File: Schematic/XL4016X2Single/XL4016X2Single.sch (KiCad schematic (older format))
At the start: 68 parts, among them J1 Solar panel, J10 SD_Micro_5V, J2 Buck1_IN, J3 LOAD, J4 Buck1_OUT, J5 Buck2_IN, J6 Buck2_OUT, J7 Battery, J8 Temperature, J9 Jack-DC, Q1 IRF4905, Q10 IRF4905, Q11 2N3906, Q12 2N3906, Q13 2N3904, Q2 IRF4905, Q3 2N3906, Q4 2N3906, Q5 2N3904, Q6 IRF4905, Q7 2N3906, Q8 2N3906, Q9 IRF4905, SW1 Backlight control, U1 XL4016_DC-DC_module, U11 DS18B20, U12 DS1307_RTC, U2 ACS712module, U3 XL4016_DC-DC_module, U4 ACS712module, U5 MP2307_DC-DC_module, U6 LCDSerial2004, U7 DS18B20, U8 ArduinoNano

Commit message: added RTC and SD to Fritzing. Minor updates to KiCad schematic.
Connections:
- net GNDPWR: no longer C1.1.2, C1.2.2, C1.3.2, C1.4.2, D3.2 (A2), J1.2 (Pin_2), J2.2 (Pin_2), J5.2 (Pin_2)
- new net SOLARGND: C1.1.2, C1.2.2, C1.3.2, C1.4.2, D3.2 (A2), J1.2 (Pin_2), J2.2 (Pin_2), J5.2 (Pin_2)
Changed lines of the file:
@@
 Sheet 1 1
 Title "XL4016X2Single"
-Date "2018-04-11"
-Rev "Initial issue"
+Date "2018-04-12"
+Rev "V2"
 Comp "farmerkeith"
 Comment1 ""
@@
 $EndComp
 $Comp
-L GNDPWR #PWR3
-U 1 1 5ACD67FC
-P 900 1250
-F 0 "#PWR3" H 900 1050 50  0001 C CNN
-F 1 "GNDPWR" H 900 1120 50  0000 C CNN
-F 2 "" H 900 1200 50  0001 C CNN
-F 3 "" H 900 1200 50  0001 C CNN
-	1    900  1250
-	1    0    0    -1
-$EndComp
-$Comp
 L GNDPWR #PWR13
 U 1 1 5ACD67FD
@@
 $EndComp
 Wire Wire Line
-	1350 1050 1850 1050
-Wire Wire Line
-	900  750  2100 750
+	1350 1050 1550 1050
+Wire Wire Line
+	1550 1050 1850 1050
+Wire Wire Line
+	900  750  1100 750
+Wire Wire Line
+	1100 750  1350 750
+Wire Wire Line
+	1350 750  2100 750
 $Comp
 L GND #PWR4
@@
 $EndComp
 $Comp
-L GNDPWR #PWR8
-U 1 1 5ACD6807
-P 3200 1950
-F 0 "#PWR8" H 3200 1750 50  0001 C CNN
-F 1 "GNDPWR" H 3200 1820 50  0000 C CNN
-F 2 "" H 3200 1900 50  0001 C CNN
-F 3 "" H 3200 1900 50  0001 C CNN
-	1    3200 1950
-	1    0    0    -1
-$EndComp
-$Comp
 L ACS712module U2
 U 1 1 5ACD6808
@@
 Connection ~ 9800 3650
 Wire Wire Line
-	2550 750  4500 750
+	2550 750  2900 750
+Wire Wire Line
+	2900 750  3400 750
+Wire Wire Line
+	3400 750  4500 750
 $Comp
 L XL4016_DC-DC_module U3
@@
 L GNDPWR #PWR1
 U 1 1 5ACD6813
-P 3800 850
-F 0 "#PWR1" H 3800 650 50  0001 C CNN
-F 1 "GNDPWR" H 3800 720 50  0000 C CNN
-F 2 "" H 3800 800 50  0001 C CNN
-F 3 "" H 3800 800 50  0001 C CNN
-	1    3800 850
-	1    0    0    -1
-$EndComp
-Wire Wire Line
-	3800 850  4500 850
-Wire Wire Line
-	4500 1050 4150 1050
-Wire Wire Line
-	4150 1050 4150 850
-Connection ~ 4150 850
+P 3800 1050
+F 0 "#PWR1" H 3800 850 50  0001 C CNN
+F 1 "GNDPWR" H 3800 920 50  0000 C CNN
+F 2 "" H 3800 1000 50  0001 C CNN
+F 3 "" H 3800 1000 50  0001 C CNN
+	1    3800 1050
+	1    0    0    -1
+$EndComp
+Wire Wire Line
+	3800 1050 4500 1050
+Wire Wire Line
+	3300 850  4500 850
 $Comp
 L GNDPWR #PWR7
 U 1 1 5ACD6814
-P 3800 1900
-F 0 "#PWR7" H 3800 1700 50  0001 C CNN
-F 1 "GNDPWR" H 3800 1770 50  0000 C CNN
-F 2 "" H 3800 1850 50  0001 C CNN
-F 3 "" H 3800 1850 50  0001 C CNN
-	1    3800 1900
-	1    0    0    -1
-$EndComp
-Wire Wire Line
-	3800 1900 4500 1900
-Wire Wire Line
-	4150 2100 4150 1900
-Connection ~ 4150 1900
-Wire Wire Line
-	4500 2100 4150 2100
+P 3800 2100
+F 0 "#PWR7" H 3800 1900 50  0001 C CNN
+F 1 "GNDPWR" H 3800 1970 50  0000 C CNN
+F 2 "" H 3800 2050 50  0001 C CNN
+F 3 "" H 3800 2050 50  0001 C CNN
+	1    3800 2100
+	1    0    0    -1
+$EndComp
+Wire Wire Line
+	3800 2100 4500 2100
+Wire Wire Line
+	3200 1900 4500 1900
 $Comp
 L D_ALT D4
@@
 Arduino_pin_D2
 Wire Wire Line
-	1050 3150 2500 3150
+	1050 3150 1950 3150
+Wire Wire Line
+	1950 3150 2350 3150
+Wire Wire Line
+	2350 3150 2500 3150
 $Comp
 L GND #PWR11
@@
 	1100 1150 1100 1250
 Wire Wire Line
+	1100 1250 1100 1350
+Wire Wire Line
 	1100 850  1100 750
 Connection ~ 1100 750
@@
 $EndComp
 Wire Wire Line
-	7700 800  9900 800
+	7700 800  7850 800
+Wire Wire Line
+	7850 800  8250 800
+Wire Wire Line
+	8250 800  9900 800
 Wire Wire Line
 	10300 800  10450 800
@@
 $EndComp
 Wire Wire Line
-	5300 5350 10600 5350
+	5300 5350 6150 5350
+Wire Wire Line
+	6150 5350 6950 5350
+Wire Wire Line
+	6950 5350 8250 5350
+Wire Wire Line
+	8250 5350 8800 5350
+Wire Wire Line
+	8800 5350 10600 5350
 $Comp
 L GND #PWR16
@@
 	7700 2200 8250 2200
 Wire Wire Line
-	7500 3550 9500 3550
-Wire Wire Line
-	8250 800  8250 3450
+	7500 3550 8800 3550
+Wire Wire Line
+	8800 3550 9500 3550
+Wire Wire Line
+	8250 800  8250 2200
+Wire Wire Line
+	8250 2200 8250 3450
 Wire Wire Line
 	6150 3850 5950 3850
@@
 	5400 3550 5950 3550
 Wire Wire Line
-	4050 3550 6250 3550
+	4050 3550 4700 3550
+Wire Wire Line
+	4700 3550 6250 3550
 Wire Wire Line
 	4700 3550 5000 3550
@@
 	4450 4850 5550 4850
 Wire Wire Line
-	6500 800  7300 800
+	6500 800  7000 800
+Wire Wire Line
+	7000 800  7300 800
 $Comp
 L GND #PWR6
@@
 $EndComp
 Wire Wire Line
-	8050 3850 8050 5050
+	8050 3850 8050 4650
+Wire Wire Line
+	8050 4650 8050 5050
 Wire Wire Line
 	6950 5150 6950 5350
@@
 	7900 5750 7900 4650
 Wire Wire Line
-	7900 4650 8250 4650
+	7900 4650 8050 4650
+Wire Wire Line
+	8050 4650 8250 4650
 Connection ~ 8050 4650
 $Comp
@@
 Arduino_pin_A6
 Wire Wire Line
-	2900 750  2900 1950
+	2900 750  2900 1000
+Wire Wire Line
+	2900 1000 2900 1300
+Wire Wire Line
+	2900 1300 2900 1650
+Wire Wire Line
+	2900 1650 2900 1950
 Connection ~ 2900 1650
 Connection ~ 2900 1300
@@
 Connection ~ 2900 1000
 Wire Wire Line
-	3200 1000 3200 1950
+	3200 1000 3200 1300
+Wire Wire Line
+	3200 1300 3200 1650
+Wire Wire Line
+	3200 1650 3200 1950
 Connection ~ 3200 1300
 Connection ~ 3200 1650
@@
 	2350 4100 3150 4100
 Wire Wire Line
-	3150 4100 3150 4400
-Wire Wire Line
-	3150 4400 1200 4400
+	3150 4400 3150 4100
+Wire Wire Line
+	1200 4400 1500 4400
+Wire Wire Line
+	1500 4400 3150 4400
 $Comp
 L DS18B20 U11
@@
 NoConn ~ 4450 7050
 NoConn ~ 4450 6950
+Text GLabel 1100 1350 0    60   Input ~ 0
+SOLARGND
+Connection ~ 1100 1250
+Wire Wire Line
+	3200 1000 3300 1000
+Wire Wire Line
+	3300 1000 3300 850
+Text GLabel 3200 2000 2    60   Input ~ 0
+SOLARGND
+Wire Wire Line
+	3200 1950 3200 2000
+Connection ~ 3200 1900
+Connection ~ 3200 1000
 $EndSCHEMATC

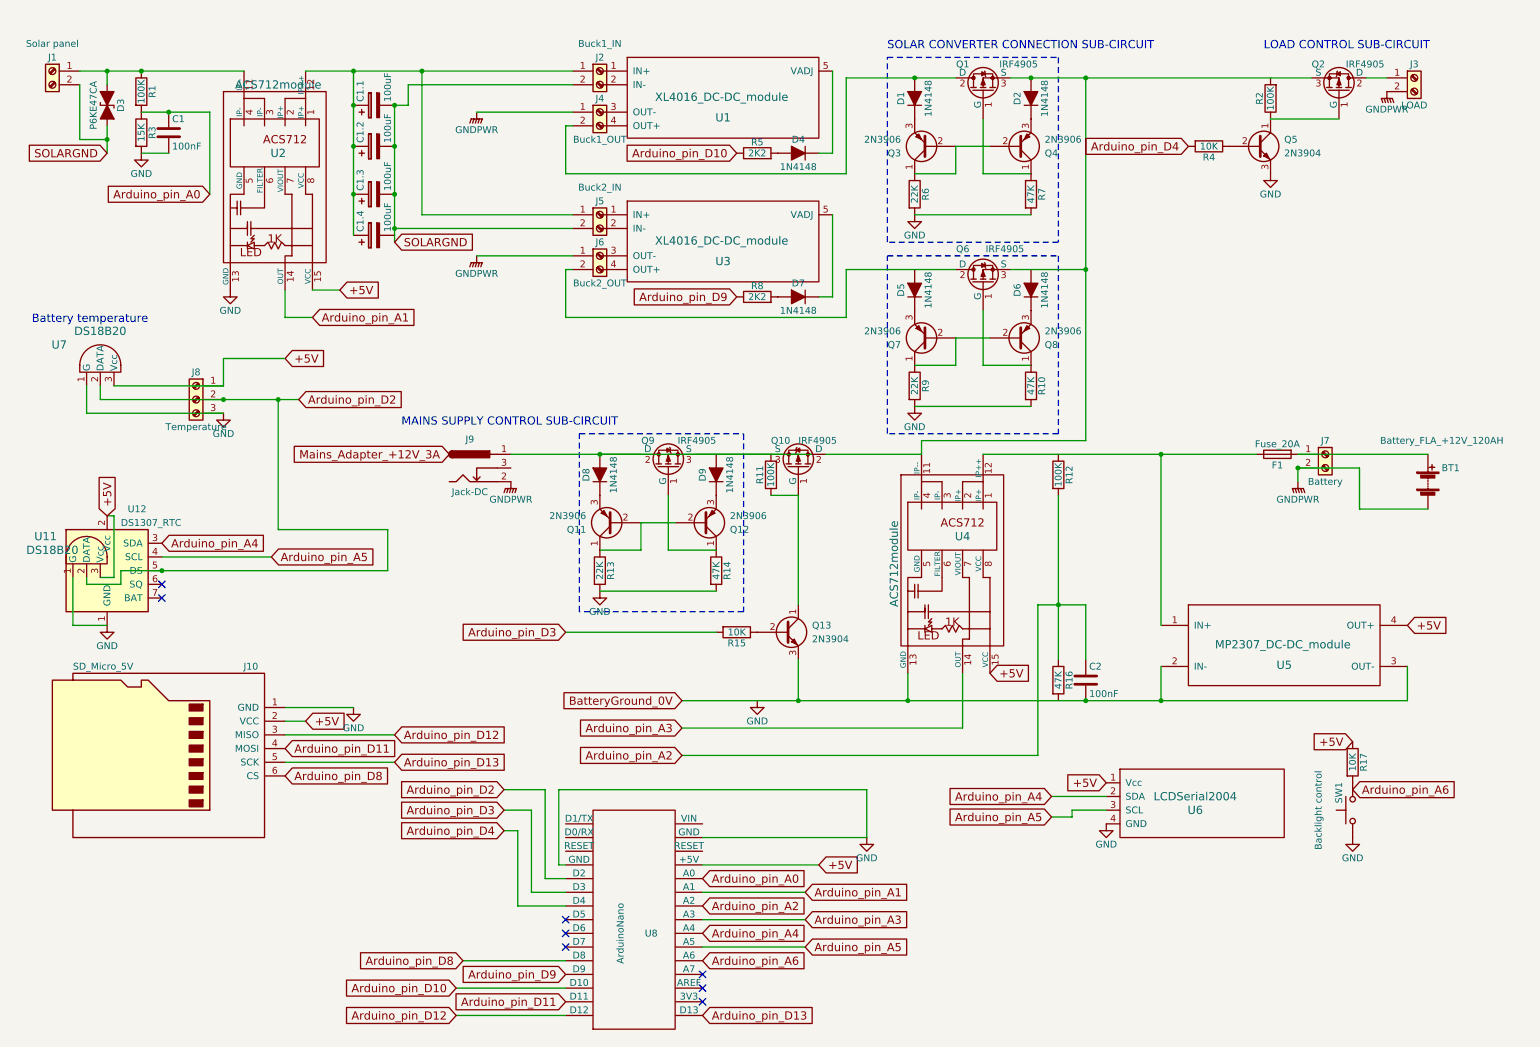
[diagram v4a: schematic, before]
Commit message: Green and Red status LEDs added
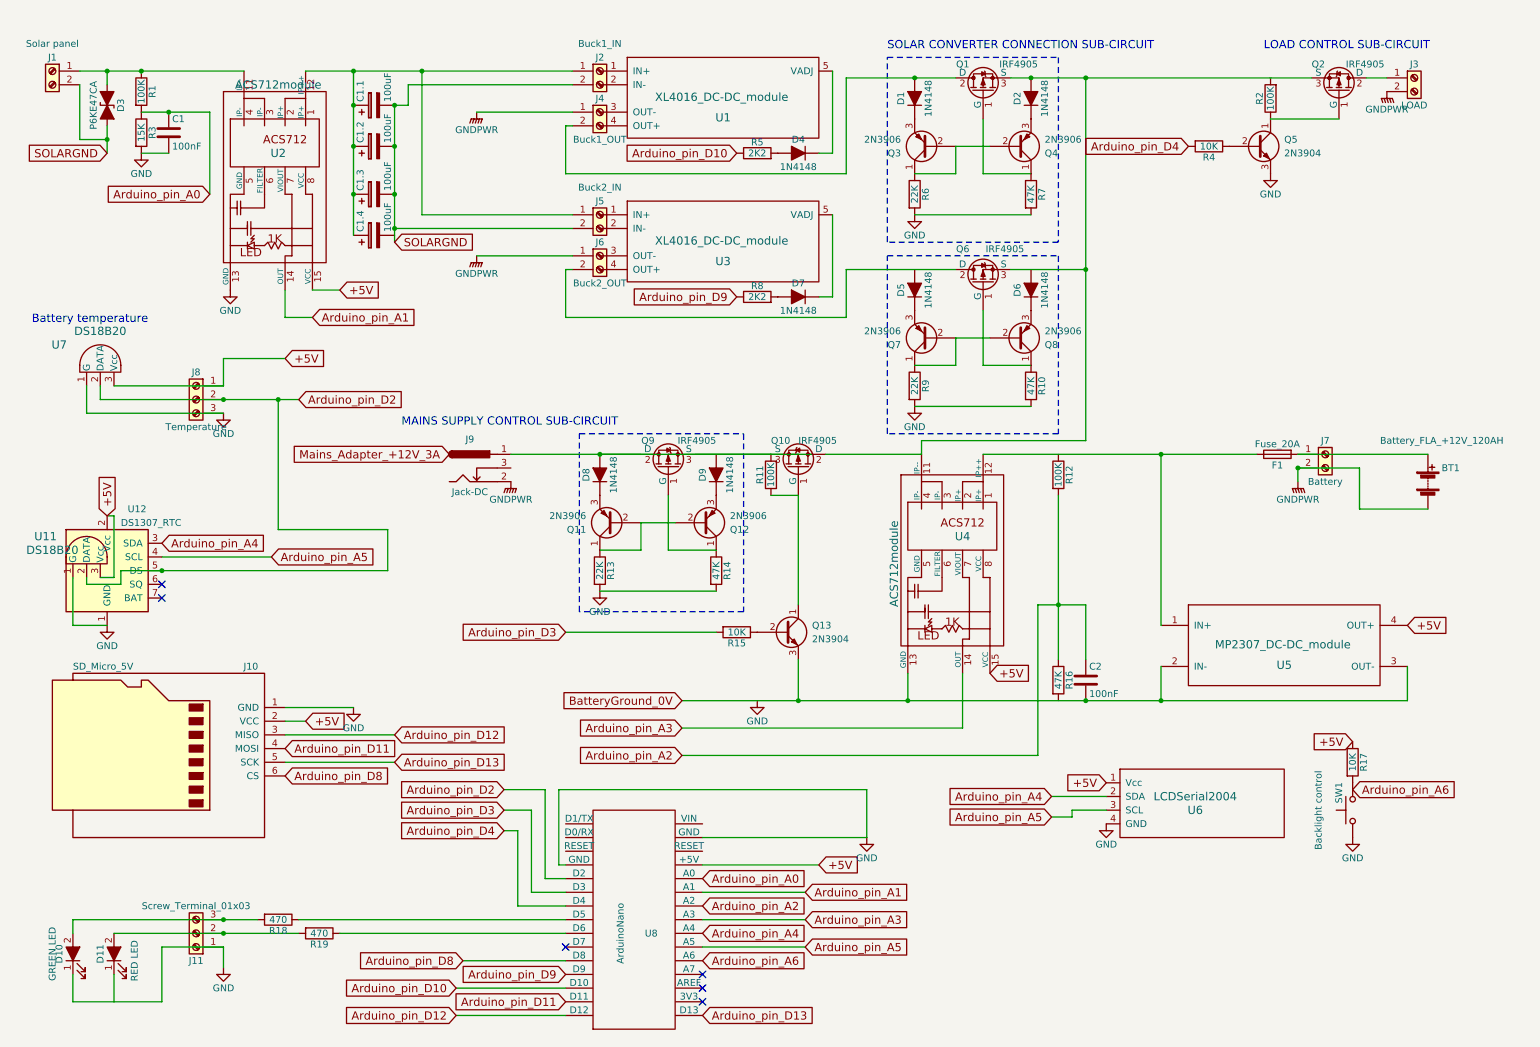
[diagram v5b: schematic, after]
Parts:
- added D10: GREEN LED, symbol LED_ALT
- added D11: RED LED, symbol LED_ALT
- added J11: Screw_Terminal_01x03, symbol Screw_Terminal_01x03
- added R18, R19: 470, symbol R
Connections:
- net GND: now also D10.1 (K), J11.1 (Pin_1)
- net SOLARGND: no longer C1.4.2
- net at U8.8 (D5): now also R18.1
- net at U8.9 (D6): now also R19.1
- new net: D11.2 (A), J11.2 (Pin_2), R19.2
- new net: D10.2 (A), J11.3 (Pin_3), R18.2
- no-connect marks 8 -> 6
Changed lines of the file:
@@
 $EndComp
 $Comp
-L GNDPWR #PWR13
+L GNDPWR #PWR11
 U 1 1 5ACD67FD
 P 9800 3750
-F 0 "#PWR13" H 9800 3550 50  0001 C CNN
+F 0 "#PWR11" H 9800 3550 50  0001 C CNN
 F 1 "GNDPWR" H 9800 3620 50  0000 C CNN
 F 2 "" H 9800 3700 50  0001 C CNN
@@
 $EndComp
 Wire Wire Line
-	1350 1050 1550 1050
-Wire Wire Line
-	1550 1050 1850 1050
-Wire Wire Line
-	900  750  1100 750
-Wire Wire Line
-	1100 750  1350 750
-Wire Wire Line
-	1350 750  2100 750
-$Comp
-L GND #PWR4
+	1350 1050 1850 1050
+Wire Wire Line
+	900  750  2100 750
+$Comp
+L GND #PWR3
 U 1 1 5ACD6801
 P 1350 1350
-F 0 "#PWR4" H 1350 1100 50  0001 C CNN
+F 0 "#PWR3" H 1350 1100 50  0001 C CNN
 F 1 "GND" H 1350 1200 50  0000 C CNN
 F 2 "" H 1350 1350 50  0001 C CNN
@@
 	9800 3650 9800 3750
 $Comp
-L GNDPWR #PWR2
+L GNDPWR #PWR1
 U 1 1 5ACD6802
 P 10450 900
-F 0 "#PWR2" H 10450 700 50  0001 C CNN
+F 0 "#PWR1" H 10450 700 50  0001 C CNN
 F 1 "GNDPWR" H 10450 770 50  0000 C CNN
 F 2 "" H 10450 850 50  0001 C CNN
@@
 $EndComp
 $Comp
-L GND #PWR9
+L GND #PWR7
 U 1 1 5ACD6809
 P 2000 2350
-F 0 "#PWR9" H 2000 2100 50  0001 C CNN
+F 0 "#PWR7" H 2000 2100 50  0001 C CNN
 F 1 "GND" H 2000 2200 50  0000 C CNN
 F 2 "" H 2000 2350 50  0001 C CNN
@@
 Connection ~ 9800 3650
 Wire Wire Line
-	2550 750  2900 750
-Wire Wire Line
-	2900 750  3400 750
-Wire Wire Line
-	3400 750  4500 750
+	2550 750  4500 750
 $Comp
 L XL4016_DC-DC_module U3
@@
 	3400 1800 4500 1800
 $Comp
-L GNDPWR #PWR1
+L GNDPWR #PWR2
 U 1 1 5ACD6813
 P 3800 1050
-F 0 "#PWR1" H 3800 850 50  0001 C CNN
+F 0 "#PWR2" H 3800 850 50  0001 C CNN
 F 1 "GNDPWR" H 3800 920 50  0000 C CNN
 F 2 "" H 3800 1000 50  0001 C CNN
@@
 	3300 850  4500 850
 $Comp
-L GNDPWR #PWR7
+L GNDPWR #PWR6
 U 1 1 5ACD6814
 P 3800 2100
-F 0 "#PWR7" H 3800 1900 50  0001 C CNN
+F 0 "#PWR6" H 3800 1900 50  0001 C CNN
 F 1 "GNDPWR" H 3800 1970 50  0000 C CNN
 F 2 "" H 3800 2050 50  0001 C CNN
@@
 Arduino_pin_D2
 Wire Wire Line
-	1050 3150 1950 3150
-Wire Wire Line
-	1950 3150 2350 3150
-Wire Wire Line
-	2350 3150 2500 3150
-$Comp
-L GND #PWR11
+	1050 3150 2500 3150
+$Comp
+L GND #PWR9
 U 1 1 5ACD681B
 P 1950 3250
-F 0 "#PWR11" H 1950 3000 50  0001 C CNN
+F 0 "#PWR9" H 1950 3000 50  0001 C CNN
 F 1 "GND" H 1950 3100 50  0000 C CNN
 F 2 "" H 1950 3250 50  0001 C CNN
@@
 	900  1250 900  850
 Wire Wire Line
-	1100 1150 1100 1250
-Wire Wire Line
-	1100 1250 1100 1350
+	1100 1150 1100 1350
 Wire Wire Line
 	1100 850  1100 750
@@
 $EndComp
 Wire Wire Line
-	7700 800  7850 800
-Wire Wire Line
-	7850 800  8250 800
-Wire Wire Line
-	8250 800  9900 800
+	7700 800  9900 800
 Wire Wire Line
 	10300 800  10450 800
 $Comp
-L GND #PWR5
+L GND #PWR4
 U 1 1 5ACD8AE0
 P 9600 1500
-F 0 "#PWR5" H 9600 1250 50  0001 C CNN
+F 0 "#PWR4" H 9600 1250 50  0001 C CNN
 F 1 "GND" H 9600 1350 50  0000 C CNN
 F 2 "" H 9600 1500 50  0001 C CNN
@@
 $EndComp
 Wire Wire Line
-	5300 5350 6150 5350
-Wire Wire Line
-	6150 5350 6950 5350
-Wire Wire Line
-	6950 5350 8250 5350
-Wire Wire Line
-	8250 5350 8800 5350
-Wire Wire Line
-	8800 5350 10600 5350
-$Comp
-L GND #PWR16
+	5300 5350 10600 5350
+$Comp
+L GND #PWR14
 U 1 1 5ACD8AE5
 P 5850 5350
-F 0 "#PWR16" H 5850 5100 50  0001 C CNN
+F 0 "#PWR14" H 5850 5100 50  0001 C CNN
 F 1 "GND" H 5850 5200 50  0000 C CNN
 F 2 "" H 5850 5350 50  0001 C CNN
@@
 	7700 2200 8250 2200
 Wire Wire Line
-	7500 3550 8800 3550
-Wire Wire Line
-	8800 3550 9500 3550
-Wire Wire Line
-	8250 800  8250 2200
-Wire Wire Line
-	8250 2200 8250 3450
+	7500 3550 9500 3550
+Wire Wire Line
+	8250 800  8250 3450
 Wire Wire Line
 	6150 3850 5950 3850
@@
 	6500 2200 7300 2200
 $Comp
-L GND #PWR10
+L GND #PWR8
 U 1 1 5ACD8AE9
 P 7000 3200
-F 0 "#PWR10" H 7000 2950 50  0001 C CNN
+F 0 "#PWR8" H 7000 2950 50  0001 C CNN
 F 1 "GND" H 7000 3050 50  0000 C CNN
 F 2 "" H 7000 3200 50  0001 C CNN
@@
 	5400 3550 5950 3550
 Wire Wire Line
-	4050 3550 4700 3550
-Wire Wire Line
-	4700 3550 6250 3550
+	4050 3550 6250 3550
 Wire Wire Line
 	4700 3550 5000 3550
 $Comp
-L GND #PWR14
+L GND #PWR12
 U 1 1 5ACD8AF1
 P 4700 4550
-F 0 "#PWR14" H 4700 4300 50  0001 C CNN
+F 0 "#PWR12" H 4700 4300 50  0001 C CNN
 F 1 "GND" H 4700 4400 50  0000 C CNN
 F 2 "" H 4700 4550 50  0001 C CNN
@@
 	4450 4850 5550 4850
 Wire Wire Line
-	6500 800  7000 800
-Wire Wire Line
-	7000 800  7300 800
-$Comp
-L GND #PWR6
+	6500 800  7300 800
+$Comp
+L GND #PWR5
 U 1 1 5ACD8AF9
 P 7000 1800
-F 0 "#PWR6" H 7000 1550 50  0001 C CNN
+F 0 "#PWR5" H 7000 1550 50  0001 C CNN
 F 1 "GND" H 7000 1650 50  0000 C CNN
 F 2 "" H 7000 1800 50  0001 C CNN
@@
 $EndComp
 Wire Wire Line
-	8050 3850 8050 4650
-Wire Wire Line
-	8050 4650 8050 5050
+	8050 3850 8050 5050
 Wire Wire Line
 	6950 5150 6950 5350
@@
 	7900 5750 7900 4650
 Wire Wire Line
-	7900 4650 8050 4650
-Wire Wire Line
-	8050 4650 8250 4650
+	7900 4650 8250 4650
 Connection ~ 8050 4650
 $Comp
@@
 	6300 6550 5450 6550
 $Comp
-L GND #PWR19
+L GND #PWR17
 U 1 1 5ACDAD3F
 P 6650 6350
-F 0 "#PWR19" H 6650 6100 50  0001 C CNN
+F 0 "#PWR17" H 6650 6100 50  0001 C CNN
 F 1 "GND" H 6650 6200 50  0000 C CNN
 F 2 "" H 6650 6350 50  0001 C CNN
@@
 +5V
 $Comp
-L GND #PWR18
+L GND #PWR16
 U 1 1 5ACDAD48
 P 8400 6250
-F 0 "#PWR18" H 8400 6000 50  0001 C CNN
+F 0 "#PWR16" H 8400 6000 50  0001 C CNN
 F 1 "GND" H 8400 6100 50  0000 C CNN
 F 2 "" H 8400 6250 50  0001 C CNN
@@
 $EndComp
 $Comp
-L GND #PWR20
+L GND #PWR18
 U 1 1 5ACDAD4A
 P 10200 6350
-F 0 "#PWR20" H 10200 6100 50  0001 C CNN
+F 0 "#PWR18" H 10200 6100 50  0001 C CNN
 F 1 "GND" H 10200 6200 50  0000 C CNN
 F 2 "" H 10200 6350 50  0001 C CNN
@@
 Arduino_pin_A6
 Wire Wire Line
-	2900 750  2900 1000
-Wire Wire Line
-	2900 1000 2900 1300
-Wire Wire Line
-	2900 1300 2900 1650
-Wire Wire Line
-	2900 1650 2900 1950
+	2900 750  2900 1950
 Connection ~ 2900 1650
 Connection ~ 2900 1300
@@
 Connection ~ 2900 1000
 Wire Wire Line
-	3200 1000 3200 1300
-Wire Wire Line
-	3200 1300 3200 1650
-Wire Wire Line
-	3200 1650 3200 1950
+	3200 1000 3200 2000
 Connection ~ 3200 1300
 Connection ~ 3200 1650
@@
 Connection ~ 4700 3550
 $Comp
-L GNDPWR #PWR12
+L GNDPWR #PWR10
 U 1 1 5AD115C3
 P 4050 3750
-F 0 "#PWR12" H 4050 3550 50  0001 C CNN
+F 0 "#PWR10" H 4050 3550 50  0001 C CNN
 F 1 "GNDPWR" H 4050 3620 50  0000 C CNN
 F 2 "" H 4050 3700 50  0001 C CNN
@@
 Arduino_pin_D8
 $Comp
-L GND #PWR17
+L GND #PWR15
 U 1 1 5AD02D7E
 P 2900 5400
-F 0 "#PWR17" H 2900 5150 50  0001 C CNN
+F 0 "#PWR15" H 2900 5150 50  0001 C CNN
 F 1 "GND" H 2900 5250 50  0000 C CNN
 F 2 "" H 2900 5400 50  0001 C CNN
@@
 +5V
 $Comp
-L GND #PWR15
+L GND #PWR13
 U 1 1 5AD046C9
 P 1100 4800
-F 0 "#PWR15" H 1100 4550 50  0001 C CNN
+F 0 "#PWR13" H 1100 4550 50  0001 C CNN
 F 1 "GND" H 1100 4650 50  0000 C CNN
 F 2 "" H 1100 4800 50  0001 C CNN
@@
 	2350 4100 3150 4100
 Wire Wire Line
-	3150 4400 3150 4100
-Wire Wire Line
-	1200 4400 1500 4400
-Wire Wire Line
-	1500 4400 3150 4400
+	3150 4100 3150 4400
+Wire Wire Line
+	3150 4400 1200 4400
 $Comp
 L DS18B20 U11
@@
 NoConn ~ 1500 4500
 NoConn ~ 1500 4600
-NoConn ~ 4450 7050
-NoConn ~ 4450 6950
 Text GLabel 1100 1350 0    60   Input ~ 0
 SOLARGND
@@
 Text GLabel 3200 2000 2    60   Input ~ 0
 SOLARGND
-Wire Wire Line
-	3200 1950 3200 2000
 Connection ~ 3200 1900
 Connection ~ 3200 1000
+$Comp
+L Screw_Terminal_01x03 J11
+U 1 1 5AD42DC0
+P 1750 7050
+F 0 "J11" H 1750 7250 50  0000 C CNN
+F 1 "Screw_Terminal_01x03" H 1750 6850 50  0000 C CNN
+F 2 "" H 1750 7050 50  0001 C CNN
+F 3 "" H 1750 7050 50  0001 C CNN
+	1    1750 7050
+	-1   0    0    1
+$EndComp
+$Comp
+L LED_ALT D10
+U 1 1 5AD45350
+P 850 7200
+F 0 "D10" H 850 7300 50  0000 C CNN
+F 1 "GREEN LED" H 850 7350 50  0000 C CNN
+F 2 "" H 850 7200 50  0001 C CNN
+F 3 "" H 850 7200 50  0001 C CNN
+	1    850  7200
+	0    -1   -1   0
+$EndComp
+$Comp
+L LED_ALT D11
+U 1 1 5AD45461
+P 1150 7200
+F 0 "D11" H 1150 7300 50  0000 C CNN
+F 1 "RED LED" H 1100 7050 50  0000 C CNN
+F 2 "" H 1150 7200 50  0001 C CNN
+F 3 "" H 1150 7200 50  0001 C CNN
+	1    1150 7200
+	0    -1   -1   0
+$EndComp
+$Comp
+L R R18
+U 1 1 5AD4572E
+P 2350 6950
+F 0 "R18" V 2430 6950 50  0000 C CNN
+F 1 "470" V 2350 6950 50  0000 C CNN
+F 2 "" V 2280 6950 50  0001 C CNN
+F 3 "" H 2350 6950 50  0001 C CNN
+	1    2350 6950
+	0    1    1    0
+$EndComp
+$Comp
+L R R19
+U 1 1 5AD457E9
+P 2650 7050
+F 0 "R19" V 2730 7050 50  0000 C CNN
+F 1 "470" V 2650 7050 50  0000 C CNN
+F 2 "" V 2580 7050 50  0001 C CNN
+F 3 "" H 2650 7050 50  0001 C CNN
+	1    2650 7050
+	0    1    1    0
+$EndComp
+Wire Wire Line
+	2500 6950 4450 6950
+Wire Wire Line
+	4450 7050 2800 7050
+Wire Wire Line
+	850  6950 2200 6950
+Wire Wire Line
+	1150 7050 2500 7050
+Connection ~ 1950 7050
+Wire Wire Line
+	850  7050 850  6950
+Connection ~ 1950 6950
+Wire Wire Line
+	850  7350 850  7550
+Wire Wire Line
+	850  7550 1500 7550
+Wire Wire Line
+	1150 7550 1150 7350
+Wire Wire Line
+	1500 7550 1500 7150
+Wire Wire Line
+	1500 7150 1950 7150
+Wire Wire Line
+	1950 7150 1950 7300
+$Comp
+L GND #PWR19
+U 1 1 5AD464B1
+P 1950 7300
+F 0 "#PWR19" H 1950 7050 50  0001 C CNN
+F 1 "GND" H 1950 7150 50  0000 C CNN
+F 2 "" H 1950 7300 50  0001 C CNN
+F 3 "" H 1950 7300 50  0001 C CNN
+	1    1950 7300
+	1    0    0    -1
+$EndComp
 $EndSCHEMATC
